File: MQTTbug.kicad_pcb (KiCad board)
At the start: 2 copper layers, 86.4 x 86.4 mm, 23 parts, among them J1 Conn_01x02, J10 Conn_01x03, J11 Conn_01x04, J12 Conn_01x03, J2 Conn_01x02, J3 Conn_01x06, J4 Conn_01x04, J5 Conn_01x04, J6 Conn_01x04, J7 Conn_01x04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

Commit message: 2023-02-08: worked on PCB layout
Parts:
- J10, J12: footprint Connector_PinSocket_2.54mm:PinSocket_1x03_P2.54mm_Vertical -> Connector_PinHeader_2.54mm:PinHeader_1x03_P2.54mm_Vertical
- moved J5 47.1 mm to (90.2, 121.9), turned to 90 degrees
- moved J4 17.7 mm to (90.2, 73.7), turned to 90 degrees
- moved J12 14.1 mm to (66.0, 106.7)
- moved SW1 14.1 mm to (66.6, 118.1)
- moved J7 11.2 mm to (71.8, 87.6)
- moved J6 7.61 mm to (58.4, 87.6)
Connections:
- net Net-(J10-Pad2) renamed /SW_PWR
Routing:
- net VCC: track 0.00 -> 101.5 mm
- net Vin-: track 0.00 -> 88.3 mm
- net +3V3: track 0.00 -> 72.4 mm
- net Vin+: track 0.00 -> 32.0 mm
- net /SW_PWR: track 0.00 -> 12.0 mm
- added copper zone on B.Cu, net GND

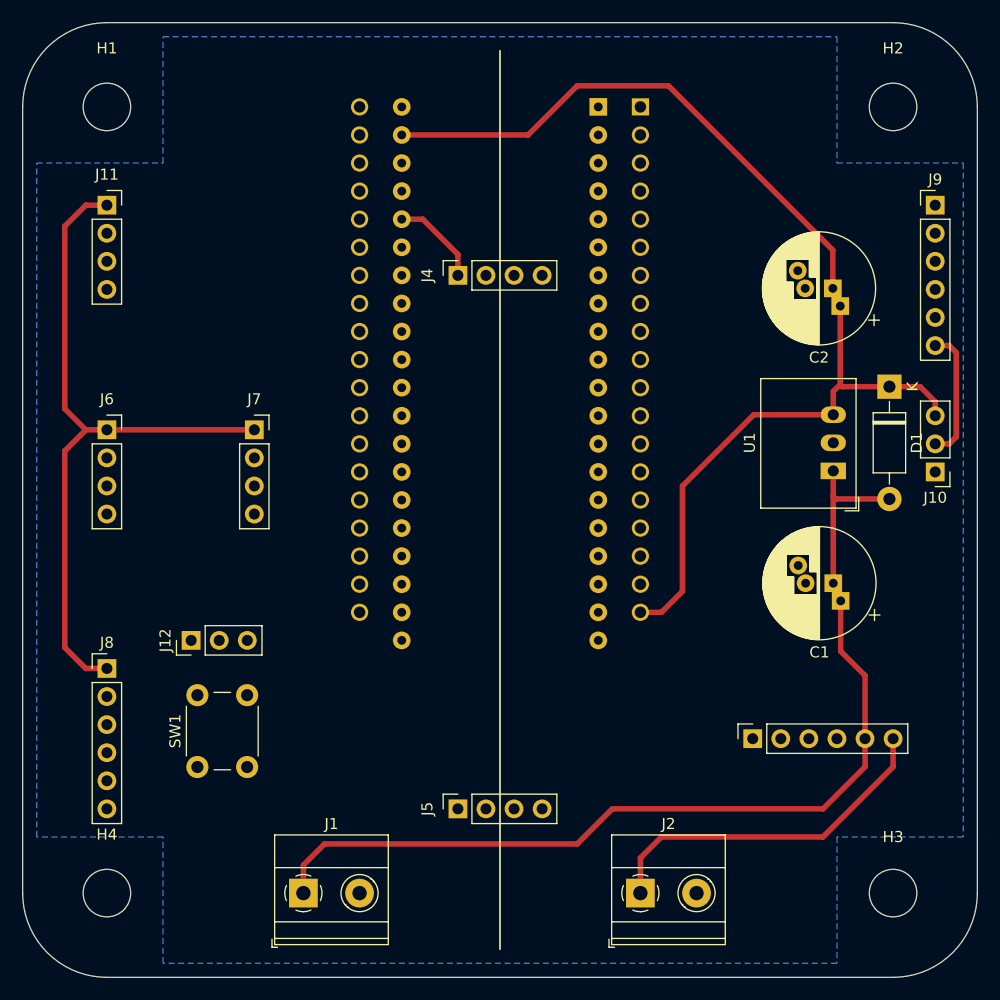
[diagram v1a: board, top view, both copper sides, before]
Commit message: Finishing board layout manual and with autorouter
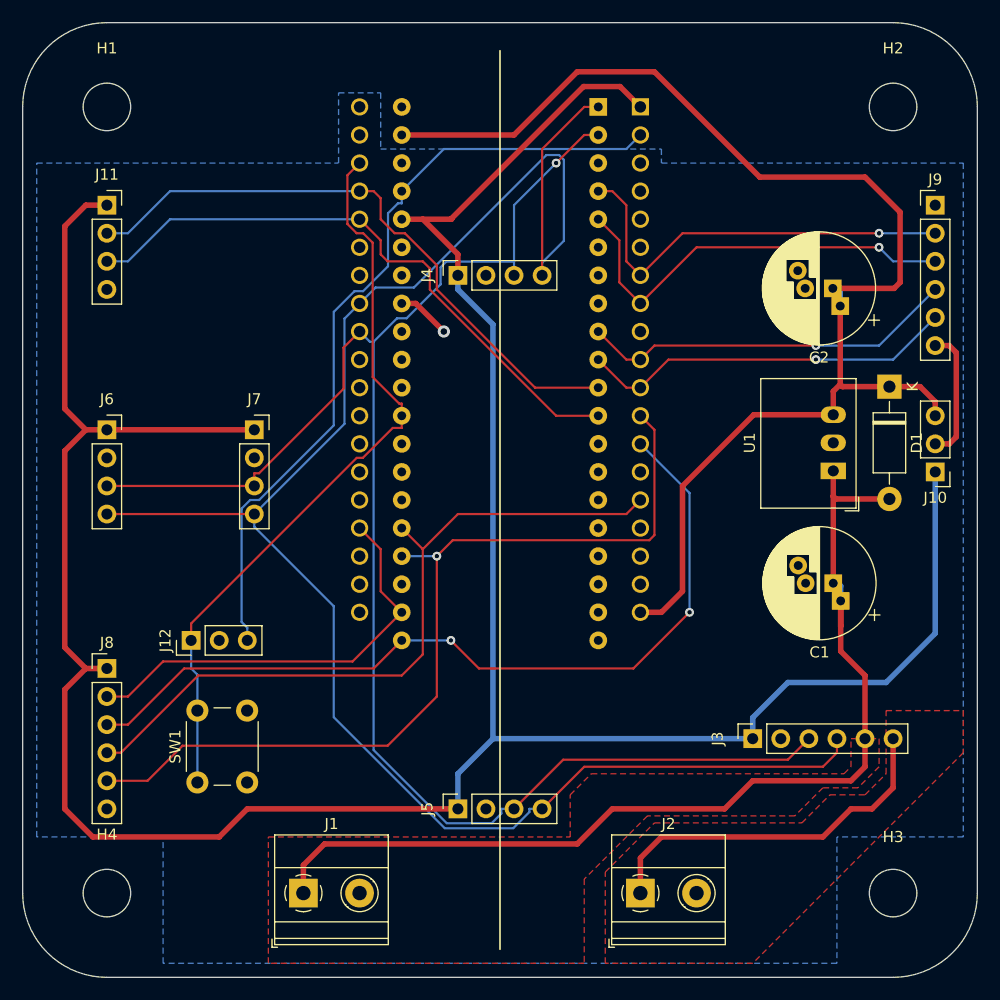
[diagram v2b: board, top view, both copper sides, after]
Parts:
- moved SW1 1.39 mm to (66.6, 119.5)
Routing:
- net +3V3: track 72.4 -> 259.6 mm
- net I2C_DA: track 0.00 -> 165.2 mm
- net I2C_CL: track 0.00 -> 148.8 mm, vias 0 -> 1
- net OWI4: track 0.00 -> 80.7 mm, vias 0 -> 1
- net OWI2: track 0.00 -> 76.1 mm, vias 0 -> 2
- net RUN: track 0.00 -> 71.7 mm
- net Pin22: track 0.00 -> 67.9 mm
- net OWI3: track 0.00 -> 66.0 mm
- net SER_TX: track 0.00 -> 55.8 mm
- net SER_RX: track 0.00 -> 55.3 mm
- net OWI1: track 0.00 -> 39.0 mm
- net SW02: track 0.00 -> 38.5 mm, vias 0 -> 1
- net SW01: track 0.00 -> 38.2 mm, vias 0 -> 1
- net SW03: track 0.00 -> 34.2 mm, vias 0 -> 1
- net SW04: track 0.00 -> 34.2 mm, vias 0 -> 1
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- added copper zone on F.Cu, net Vin+
- added copper zone on F.Cu, net Vin-

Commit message: last mods and first Gerber to PCB manufacturer
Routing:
- net GND: track 4.86 -> 38.8 mm, vias 1 -> 4
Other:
- rule pad_to_mask_clearance: 0.1 -> 0
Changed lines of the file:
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@@
       (dielectric_constraints no)
     )
-    (pad_to_mask_clearance 0.1)
-    (solder_mask_min_width 0.1)
+    (pad_to_mask_clearance 0)
     (aux_axis_origin 50.8 50.8)
     (grid_origin 50.8 50.8)
     (pcbplotparams
-      (layerselection 0x00010fc_ffffffff)
+      (layerselection 0x00010f0_ffffffff)
       (disableapertmacros false)
-      (usegerberextensions false)
-      (usegerberattributes true)
-      (usegerberadvancedattributes true)
-      (creategerberjobfile true)
+      (usegerberextensions true)
+      (usegerberattributes false)
+      (usegerberadvancedattributes false)
+      (creategerberjobfile false)
       (svguseinch false)
       (svgprecision 6)
@@
       (psa4output false)
       (plotreference true)
-      (plotvalue true)
+      (plotvalue false)
       (plotinvisibletext false)
       (sketchpadsonfab false)
-      (subtractmaskfromsilk false)
+      (subtractmaskfromsilk true)
       (outputformat 1)
       (mirror false)
-      (drillshape 1)
+      (drillshape 0)
       (scaleselection 1)
-      (outputdirectory "")
+      (outputdirectory "Gerber/")
     )
   )
@@
   (gr_arc (start 58.42 137.16) (mid 53.031846 134.928154) (end 50.8 129.54) (layer "Edge.Cuts") (width 0.1))
   (gr_line (start 137.16 58.42) (end 137.16 129.54) (layer "Edge.Cuts") (width 0.1))
+  (dimension (type aligned) (layer "Cmts.User")
+    (pts (xy 50.8 58.42) (xy 137.16 58.42))
+    (height -17.78)
+    (gr_text "86,3600 mm" (at 93.98 38.84) (layer "Cmts.User")
+      (effects (font (size 1.5 1.5) (thickness 0.3)))
+    )
+    (format (units 3) (units_format 1) (precision 4))
+    (style (thickness 0.2) (arrow_length 1.27) (text_position_mode 0) (extension_height 0.58642) (extension_offset 0.5) keep_text_aligned)
+  )
+  (dimension (type aligned) (layer "Cmts.User")
+    (pts (xy 58.42 50.8) (xy 58.42 137.16))
+    (height 18.415)
+    (gr_text "86,3600 mm" (at 38.205 93.98 90) (layer "Cmts.User")
+      (effects (font (size 1.5 1.5) (thickness 0.3)))
+    )
+    (format (units 3) (units_format 1) (precision 4))
+    (style (thickness 0.2) (arrow_length 1.27) (text_position_mode 0) (extension_height 0.58642) (extension_offset 0.5) keep_text_aligned)
+  )
   (segment (start 127 118.11) (end 127 115.57) (width 0.5) (layer "F.Cu") (net 1))
   (segment (start 127 109.855) (end 127 115.57) (width 0.5) (layer "F.Cu") (net 1))
@@
   (segment (start 124.7984 103.107) (end 124.7984 101.7569) (width 0.5) (layer "B.Cu") (net 1))
   (segment (start 124.3774 101.7569) (end 124.1275 101.507) (width 0.5) (layer "B.Cu") (net 1))
+  (segment (start 92.71 121.92) (end 92.71 118.745) (width 0.5) (layer "F.Cu") (net 2))
   (segment (start 85.09 76.2) (end 86.36 76.2) (width 0.5) (layer "F.Cu") (net 2))
   (segment (start 86.36 76.2) (end 88.9 78.74) (width 0.5) (layer "F.Cu") (net 2))
+  (segment (start 102.87 101.6) (end 90.17 101.6) (width 0.5) (layer "F.Cu") (net 2))
+  (segment (start 92.71 118.745) (end 88.9 114.935) (width 0.5) (layer "F.Cu") (net 2))
+  (segment (start 102.87 88.9) (end 90.17 88.9) (width 0.5) (layer "F.Cu") (net 2))
+  (via (at 90.17 88.9) (size 1.1) (drill 0.6) (layers "F.Cu" "B.Cu") (net 2))
+  (via (at 88.9 114.935) (size 1.1) (drill 0.6) (layers "F.Cu" "B.Cu") (net 2))
+  (via (at 90.17 101.6) (size 1.1) (drill 0.6) (layers "F.Cu" "B.Cu") (net 2))
   (via (at 88.9 78.74) (size 1.1) (drill 0.6) (layers "F.Cu" "B.Cu") (net 2))
   (segment (start 106.68 129.54) (end 106.68 126.365) (width 0.5) (layer "F.Cu") (net 3))
